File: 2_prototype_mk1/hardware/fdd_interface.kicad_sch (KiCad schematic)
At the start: 4 parts, among them J2 Conn_02x17_Odd_Even, U1 74AHCT245

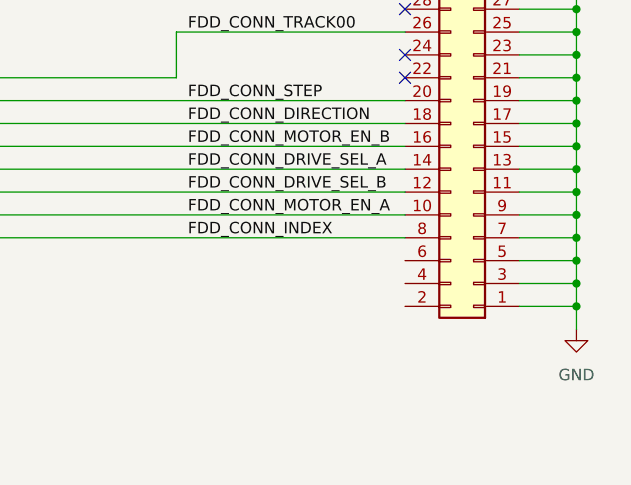
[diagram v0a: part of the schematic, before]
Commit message: Split power into own schematic
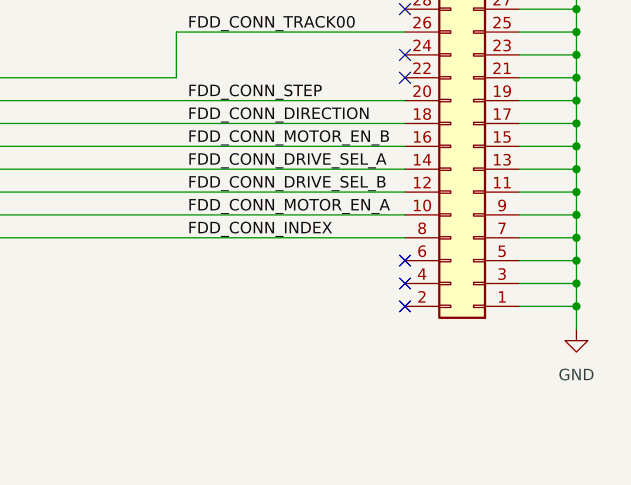
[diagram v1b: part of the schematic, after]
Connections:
- no-connect marks 6 -> 9
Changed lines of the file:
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@@
+	)
+	(no_connect
+		(at 212.09 107.95)
+	)
+	(no_connect
+		(at 212.09 105.41)
 	)
 	(no_connect
@@
 	)
 	(no_connect
+		(at 212.09 110.49)
+	)
+	(no_connect

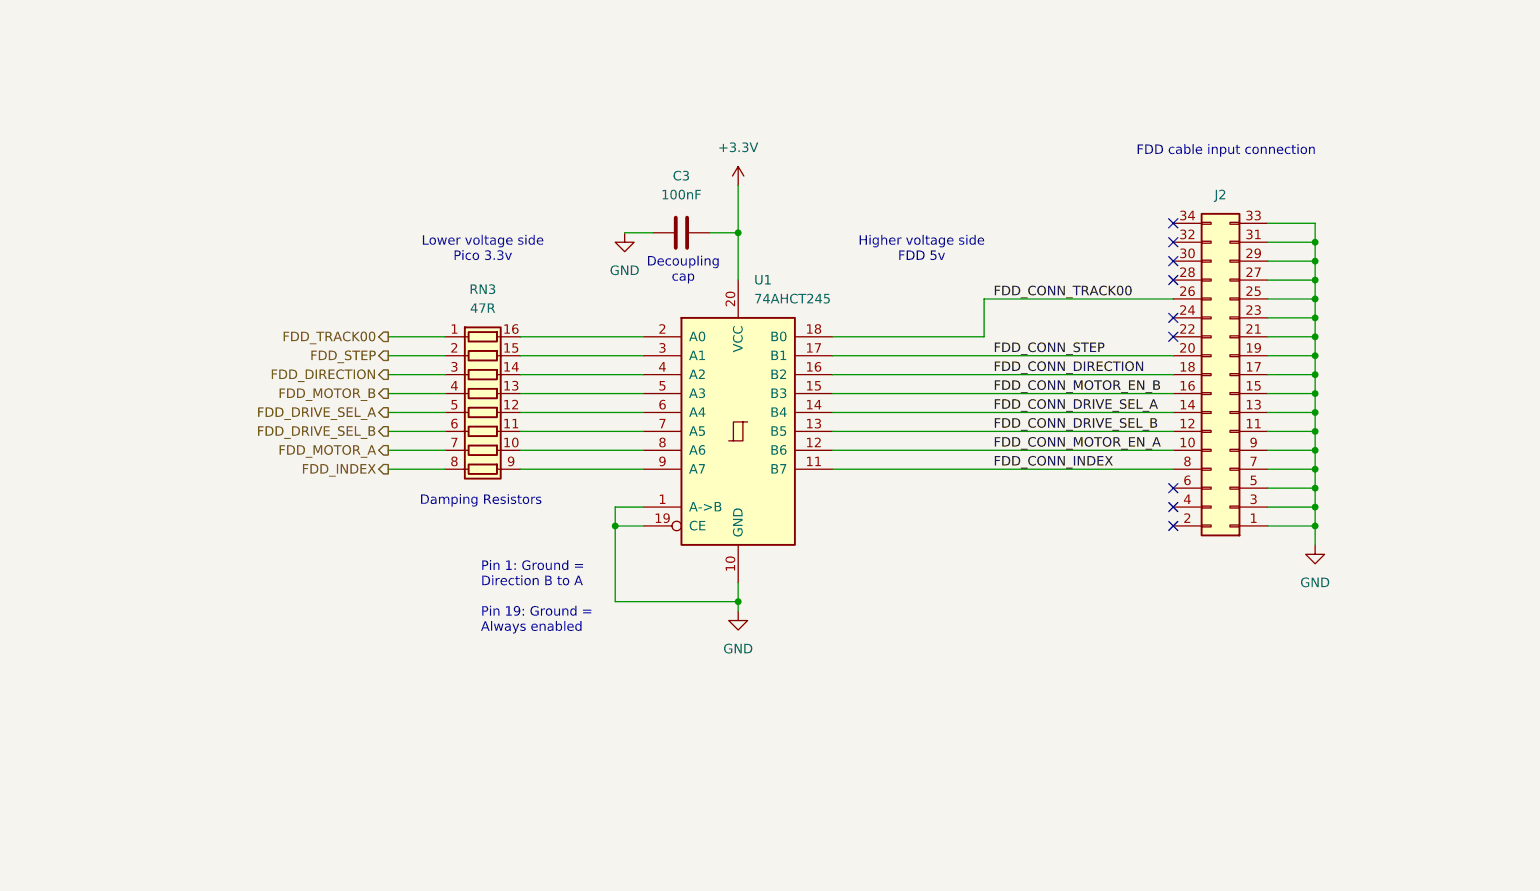
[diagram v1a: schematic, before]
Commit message: Change power connector and reroute amp
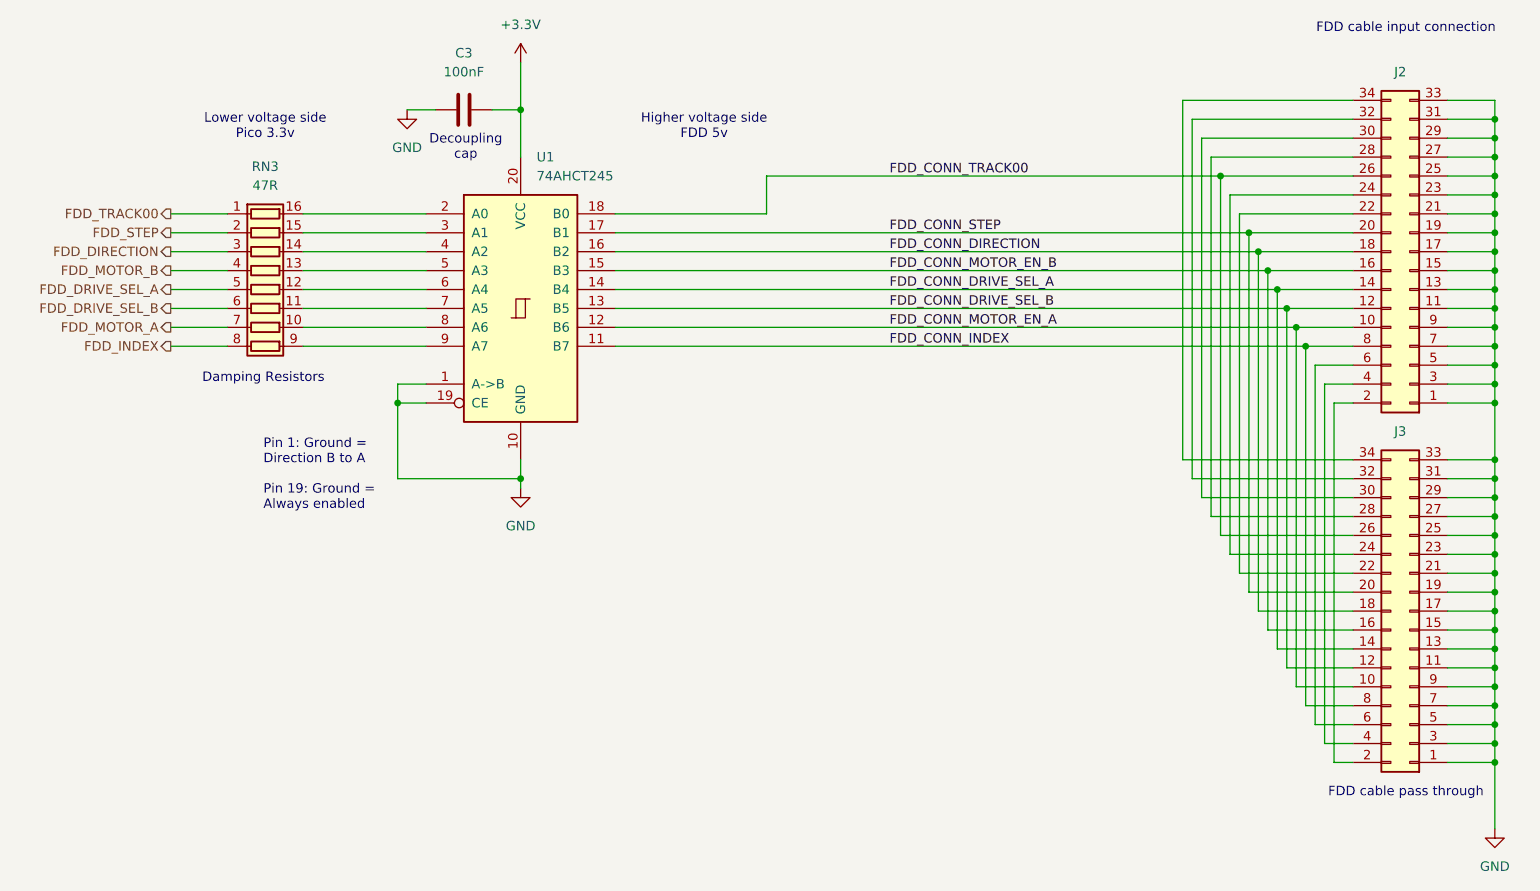
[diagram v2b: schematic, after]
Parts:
- added J3: Conn_02x17_Odd_Even, Connector_IDC:IDC-Header_2x17_P2.54mm_Vertical, symbol Connector_Generic:Conn_02x17_Odd_Even
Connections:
- net FDD_CONN_DIRECTION: now also J3.18 (Pin_18)
- net FDD_CONN_DRIVE_SEL_A: now also J3.14 (Pin_14)
- net FDD_CONN_DRIVE_SEL_B: now also J3.12 (Pin_12)
- net FDD_CONN_INDEX: now also J3.8 (Pin_8)
- net FDD_CONN_MOTOR_EN_A: now also J3.10 (Pin_10)
- net FDD_CONN_MOTOR_EN_B: now also J3.16 (Pin_16)
- net FDD_CONN_STEP: now also J3.20 (Pin_20)
- net FDD_CONN_TRACK00: now also J3.26 (Pin_26)
- net GND: now also J3.1 (Pin_1), J3.11 (Pin_11), J3.13 (Pin_13), J3.15 (Pin_15), J3.17 (Pin_17), J3.19 (Pin_19), J3.21 (Pin_21), J3.23 (Pin_23), J3.25 (Pin_25), J3.27 (Pin_27), J3.29 (Pin_29), J3.3 (Pin_3), J3.31 (Pin_31), J3.33 (Pin_33), J3.5 (Pin_5), J3.7 (Pin_7), J3.9 (Pin_9)
- net at J2.2 (Pin_2): now also J3.2 (Pin_2)
- net at J2.22 (Pin_22): now also J3.22 (Pin_22)
- net at J2.24 (Pin_24): now also J3.24 (Pin_24)
- net at J2.28 (Pin_28): now also J3.28 (Pin_28)
- net at J2.30 (Pin_30): now also J3.30 (Pin_30)
- net at J2.32 (Pin_32): now also J3.32 (Pin_32)
- net at J2.34 (Pin_34): now also J3.34 (Pin_34)
- net at J2.4 (Pin_4): now also J3.4 (Pin_4)
- net at J2.6 (Pin_6): now also J3.6 (Pin_6)
- no-connect marks 9 -> 0
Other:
- note added: "FDD cable pass through"
- moved on the sheet: C3, J2, RN3, U1
